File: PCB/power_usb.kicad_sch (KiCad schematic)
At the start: 29 parts, among them J1 USB_C_Receptacle, U1 LP2985-3.3, U3 CP2102N-A02-GQFN24, U5 LP2985-3.3

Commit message: Schematic: US resistor symbols, decoupling caps at their ICs, drop finalized VERIFY notes
- Device:R_Small -> Device:R_Small_US on all 30 resistors (same pin geometry; refs/values/fields/footprints/LCSC unchanged)
- Move label-connected decoupling caps next to their ICs: C10/C11 + C12/C13 at U3, C15/C16 at U4, C4 at U2
- Add PCB placement notes by U1, U5, U3, U4, U2/X1 and DS1 (pins from netlist)
- Remove VERIFY note lines and VERIFY fields for items Jason finalized:
  J1 D1 C10 U3 FB2 DS1 C17 SW1 X1 C100 R101 L1 C105
- Netlist identical to 4963a6d; ERC 0 errors
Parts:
- C10: VERIFY LCSC stock low; fallback C49678 (0805) per PLAN -> (none)
- D1: VERIFY Pin-to-line mapping (D-/D+/VBUS on pins 2/3/4) to be checke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 -> (none)
- FB2: VERIFY Bead or series R (<=6 ohm upper bound, PLAN 4a); value to b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 -> (none)
- J1: VERIFY UART adapter schematic pairs GCT USB4105 footprint with thi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 -> (none)
- R1, R2, R7, R8, R9: symbol Device:R_Small -> Device:R_Small_US
- U3: VERIFY Unused CP2102N pins left NC (adapter used DTR via JP1, TRRS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 -> (none)
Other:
- note added: "PCB: C1 1u at U1 pin 1, C2 100n at pin 4 (BP), C3 4.7u at pin 5; GND via at each pad."
- note added: "PCB: C10 100n + C11 4.7u at U3 pin 7 (VREGIN); C13 100n + C12 4.7u at U3 pin 6 (VDD) / pin 5 (VIO). 100n closest. GND to pin 2 / EP (25) with vias at pads."
- note added: "PCB: C7 1u at U5 pin 1, C8 100n at pin 4 (BP), C9 4.7u at pin 5; GND via at each pad."
- note added: "VERIFY (unconfirmed items on this sheet): - R9: PLAN says /RST pull-up to VBUS (as on adapter); CP2102N RST max is VIO-referenced - confirm adapter really ties to VBUS. - C22: OLED bulk value: PLAN start point 2x4.7u, tune by measurement - C24: DNP 1206 site for larger OLED bulk cap; value/part not chosen"
- note removed: "VERIFY (unconfirmed items on this sheet): - J1: UART adapter schematic pairs GCT USB4105 footprint with this HCTL LCSC part; HCTL footprint used here - confirm. Shield to GND assumed (not stated in PLAN). - D1: Pin-to-line mapping (D-/D+/VBUS on pins 2/3/4) to be checked against adapter layout. - C10: LCSC stock low; fallback C49678 (0805) per PLAN - U3: Unused CP2102N pins left NC (adapter used 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"
- moved on the sheet: C10, C11, C12, C13

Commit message: Resolve VERIFY directives: R9 to VIO, R29 on PB4, OLED bulk, SMD UPDI parts, 4.7k I2C, 0805 0R, Etherkit SMA footprint
- R9 /RST pull-up moved from +5V to CP_VDD (CP2102N DS 2.1, Table 3.10)
- New R29 1k (C21190) between C14 and PB4 to limit DTR-rise injection current (ATtiny3226 DS Table 33-1)
- C24 fitted 22u 1206 (C12891); C22/C23 kept 2x4.7u
- R13 0603 C23179, D4 1N5711W SOD-123 C154843, J5 1x4 pin header C124378
- R27/R28 4.7k C17673; R100/R120/R140 0805 0R C17477; R101/R121/R141 LCSC C17437 (DNP)
- J2-J4 footprint EtherkitKicadLibrary:SMA-ENDLAUNCH
- H1-H4 and solder jumpers excluded from BOM
- Finalized VERIFY notes removed from sheets; VERIFY.md items ticked with KiCad EE notes
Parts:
- C24: value DNP -> 22u; LCSC (none) -> C12891; MPN (none) -> CL31A226KAHNNNE; Manufacturer (none) -> Samsung; now fitted
- H1, H2, H3, H4: now left out of the parts list
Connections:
- net +5V: no longer R9.1
- net CP_VDD: now also R9.1
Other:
- note removed: "VERIFY (unconfirmed items on this sheet): - R9: PLAN says /RST pull-up to VBUS (as on adapter); CP2102N RST max is VIO-referenced - confirm adapter really ties to VBUS. - C22: OLED bulk value: PLAN start point 2x4.7u, tune by measurement - C24: DNP 1206 site for larger OLED bulk cap; value/part not chosen"
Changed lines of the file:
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@@
 		)
 	)
-	(text "VERIFY (unconfirmed items on this sheet):\n- R9: PLAN says /RST pull-up to VBUS (as on adapter); CP2102N RST max is VIO-referenced - confirm adapter really ties to\n   VBUS.\n- C22: OLED bulk value: PLAN start point 2x4.7u, tune by measurement\n- C24: DNP 1206 site for larger OLED bulk cap; value/part not chosen"
-		(exclude_from_sim no)
-		(at 230 150 0)
-		(effects
-			(font
-				(size 1 1)
-			)
-			(justify left top)
-		)
-	)
 	(text "PCB: C10 100n + C11 4.7u at U3 pin 7 (VREGIN); C13 100n + C12 4.7u at\nU3 pin 6 (VDD) / pin 5 (VIO). 100n closest. GND to pin 2 / EP (25) with vias at pads."
 		(exclude_from_sim no)
@@
 	)
 	(label "CP_VDD"
+		(at 137.16 57.15 90)
+		(effects
+			(font
+				(size 1.27 1.27)
+			)
+			(justify left bottom)
+		)
+	)
+	(label "CP_VDD"
 		(at 245.11 44.45 0)
 		(effects
@@
 		(on_board yes)
 		(in_pos_files yes)
-		(dnp yes)
+		(dnp no)
 		(property "Reference" "C24"
 			(at 187.22 261.02 0)
@@
 			)
 		)
-		(property "Value" "DNP"
+		(property "Value" "22u"
 			(at 187.22 263.22 0)
 			(show_name no)
@@
 			)
 		)
+		(property "LCSC" "C12891"
+			(at 185.42 261.62 0)
+			(hide yes)
+			(show_name no)
+			(do_not_autoplace no)
+			(effects
+				(font
+					(size 1.27 1.27)
+				)
+			)
+		)
+		(property "MPN" "CL31A226KAHNNNE"
+			(at 185.42 261.62 0)
+			(hide yes)
+			(show_name no)
+			(do_not_autoplace no)
+			(effects
+				(font
+					(size 1.27 1.27)
+				)
+			)
+		)
+		(property "Manufacturer" "Samsung"
+			(at 185.42 261.62 0)
+			(hide yes)
+			(show_name no)
+			(do_not_autoplace no)
+			(effects
+				(font
+					(size 1.27 1.27)
+				)
+			)
+		)
 		(pin "1"
 		)
@@
 		(body_style 1)
 		(exclude_from_sim no)
-		(in_bom yes)
+		(in_bom no)
 		(on_board yes)
 		(in_pos_files yes)
@@
 	)
 	(symbol
-		(lib_id "power:+5V")
-		(at 137.16 57.15 0)
-		(unit 1)
-		(body_style 1)
-		(exclude_from_sim no)
-		(in_bom no)
-		(on_board yes)
-		(in_pos_files yes)
-		(dnp no)
-		(property "Reference" "#PWR016"
-			(at 137.16 57.15 0)
-			(hide yes)
-			(show_name no)
-			(do_not_autoplace no)
-			(effects
-				(font
-					(size 1.27 1.27)
-				)
-			)
-		)
-		(property "Value" "+5V"
-			(at 137.16 53.34 0)
-			(show_name no)
-			(do_not_autoplace no)
-			(effects
-				(font
-					(size 1.27 1.27)
-				)
-			)
-		)
-		(property "Footprint" ""
-			(at 137.16 57.15 0)
-			(hide yes)
-			(show_name no)
-			(do_not_autoplace no)
-			(effects
-				(font
-					(size 1.27 1.27)
-				)
-			)
-		)
-		(property "Datasheet" ""
-			(at 137.16 57.15 0)
-			(hide yes)
-			(show_name no)
-			(do_not_autoplace no)
-			(effects
-				(font
-					(size 1.27 1.27)
-				)
-			)
-		)
-		(property "Description" ""
-			(at 137.16 57.15 0)
-			(show_name no)
-			(do_not_autoplace no)
-			(effects
-				(font
-					(size 1.27 1.27)
-				)
-			)
-		)
-		(pin "1"
-		)
-		(instances
-			(project "Si5351AVFO"
-				(path "/a0000000-0000-4000-8000-000000000001/b0000000-0000-4000-8000-000000000002"
-					(reference "#PWR016")
-					(unit 1)
-				)
-			)
-		)
-	)
-	(symbol
 		(lib_id "power:GND")
 		(at 149.86 82.55 0)
@@
 		(body_style 1)
 		(exclude_from_sim no)
-		(in_bom yes)
+		(in_bom no)
 		(on_board yes)
 		(in_pos_files yes)
@@
 		(body_style 1)
 		(exclude_from_sim no)
-		(in_bom yes)
+		(in_bom no)
 		(on_board yes)
 		(in_pos_files yes)
@@
 		(body_style 1)
 		(exclude_from_sim no)
-		(in_bom yes)
+		(in_bom no)
 		(on_board yes)
 		(in_pos_files yes)

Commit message: Pre-layout: project-local Etherkit libs (ERC 0/0), DS1/J2-J4/X1 fit review, title block, clear finalized VERIFY fields, LPF closed
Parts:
- C22: VERIFY OLED bulk value: PLAN start point 2x4.7u, tune by measureme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 -> (none)
- C24: VERIFY DNP 1206 site for larger OLED bulk cap; value/part not chos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 -> (none)
- R9: VERIFY PLAN says /RST pull-up to VBUS (as on adapter); CP2102N RST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 -> (none)
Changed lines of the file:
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@@
 		(rev "A")
 		(company "Etherkit / NT7S")
-		(comment 1 "Draft schematic, not reviewed. See VERIFY notes.")
+		(comment 1 "Draft schematic, not reviewed. Open items: docs/VERIFY.md")
 	)
 	(text "U1: +3V3D (MCU) and, via FB1, +3V3_CLK (Si5351 + TCXO). Rev F U1/C1/C2/C3."
@@
 			)
 		)
-		(property "VERIFY" "DNP 1206 site for larger OLED bulk cap; value/part not chosen"
-			(at 185.42 261.62 0)
-			(hide yes)
-			(show_name no)
-			(do_not_autoplace no)
-			(effects
-				(font
-					(size 1.27 1.27)
-				)
-			)
-		)
 		(property "LCSC" "C12891"
 			(at 185.42 261.62 0)
@@
 			)
 		)
-		(property "VERIFY" "OLED bulk value: PLAN start point 2x4.7u, tune by measurement"
-			(at 160.02 261.62 0)
-			(hide yes)
-			(show_name no)
-			(do_not_autoplace no)
-			(effects
-				(font
-					(size 1.27 1.27)
-				)
-			)
-		)
 		(pin "1"
 		)
@@
 			(at 137.16 59.69 0)
 			(hide yes)
-			(show_name no)
-			(do_not_autoplace no)
-			(effects
-				(font
-					(size 1.27 1.27)
-				)
-			)
-		)
-		(property "VERIFY" "PLAN says /RST pull-up to VBUS (as on adapter); CP2102N RST max is VIO-referenced - confirm adapter really ties to VBUS."
-			(at 137.16 59.69 0)
-			(hide yes)

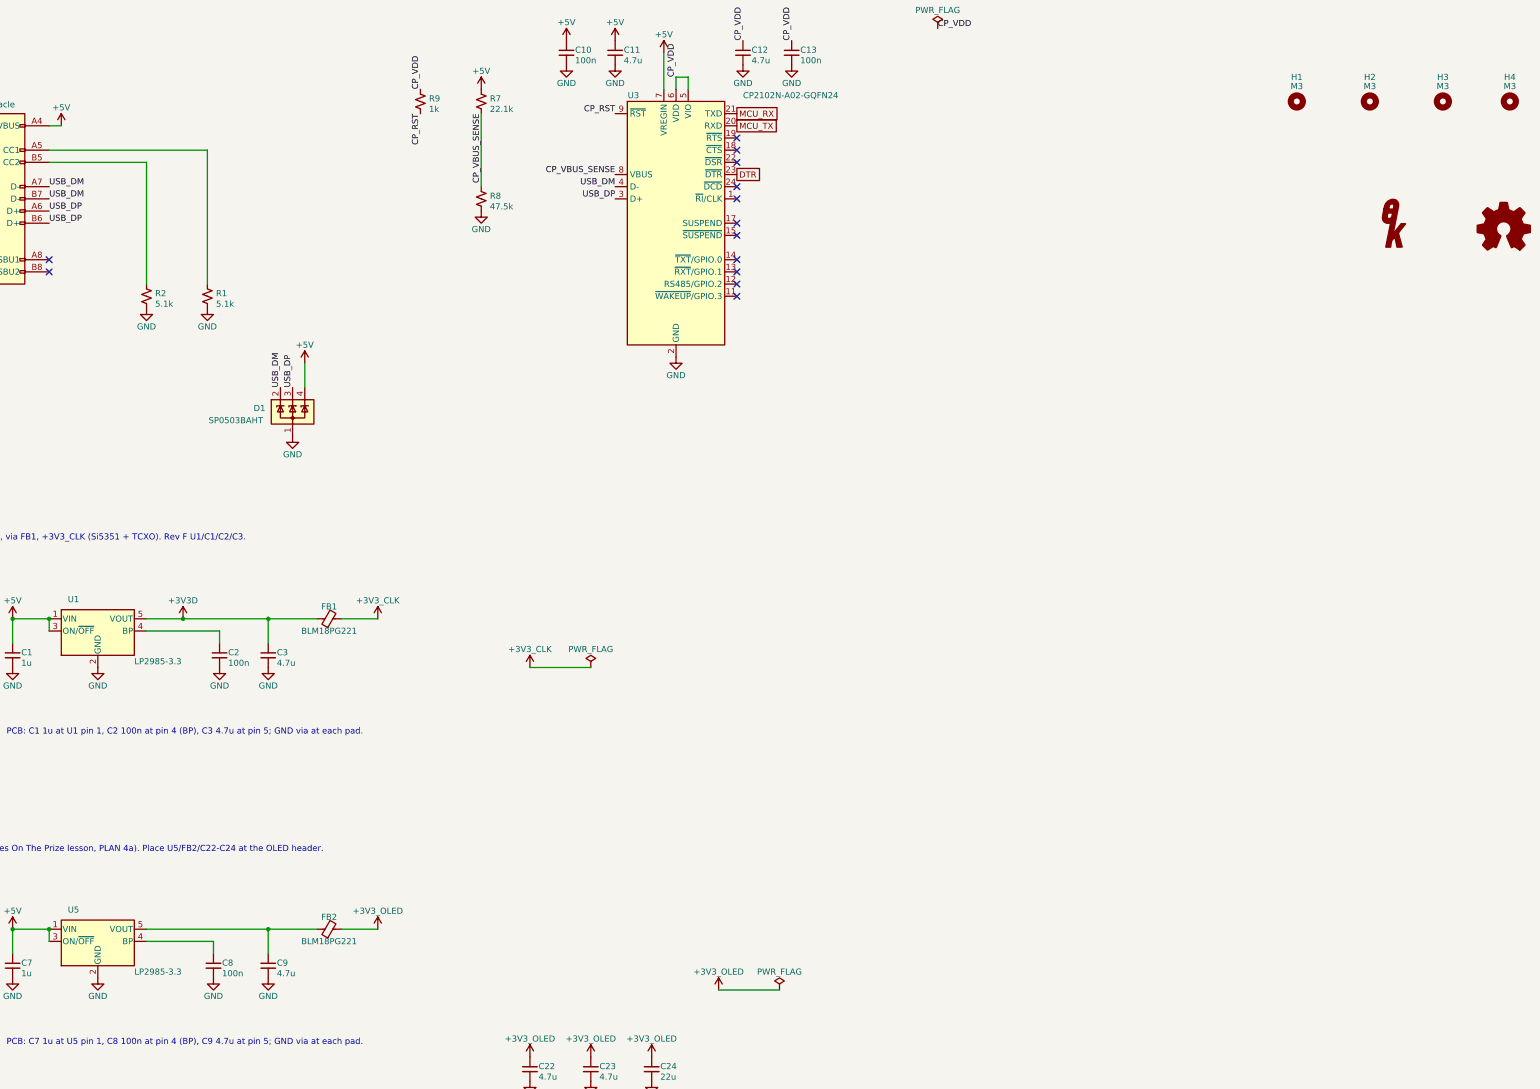
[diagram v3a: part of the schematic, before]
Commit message: H1-H4: plated M3 mounting holes (MountingHole_3.2mm_M3_Pad_Via) tied to GND
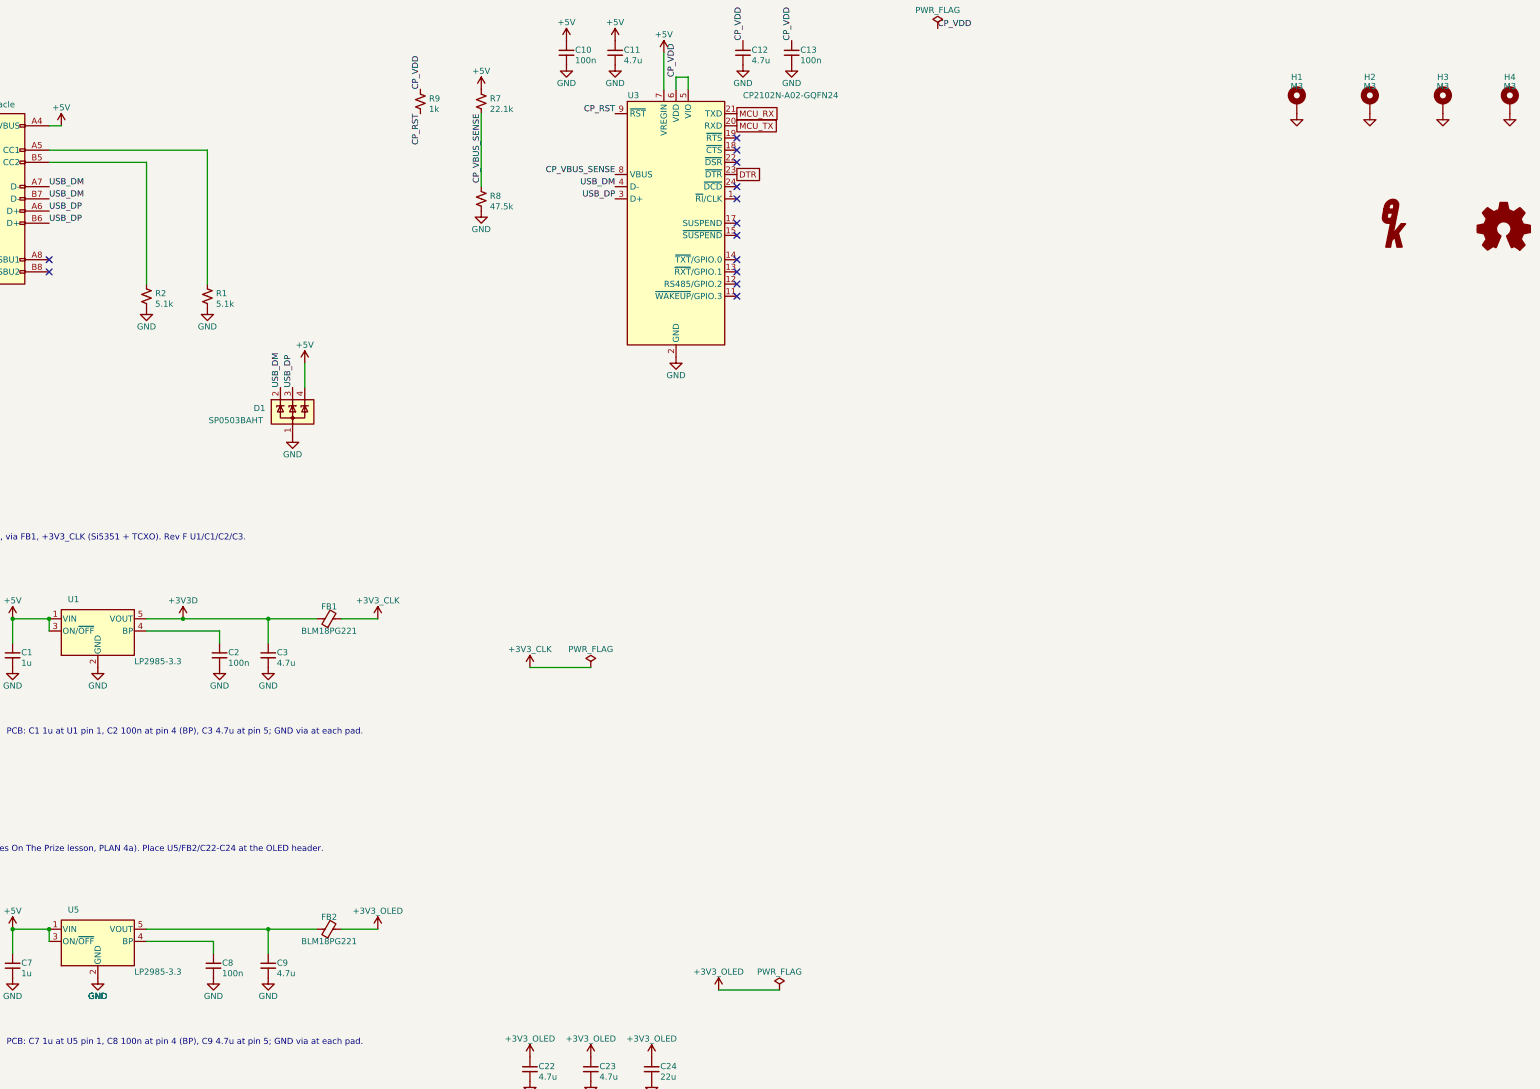
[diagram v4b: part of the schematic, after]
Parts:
- H1, H2, H3, H4: footprint MountingHole:MountingHole_3.2mm_M3 -> MountingHole:MountingHole_3.2mm_M3_Pad_Via; symbol Mechanical:MountingHole -> Mechanical:MountingHole_Pad
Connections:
- net GND: now also H1.1, H2.1, H3.1, H4.1
